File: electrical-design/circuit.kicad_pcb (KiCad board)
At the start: 4 copper layers, 90 x 70 mm, 53 parts, among them J1 AVR-ISP-6, Q1 2N3906, Q2 2N3906, Q3 2N3906, Q4 2N3906, SW1 Reset Button, SW2 DS02C-254-1L-04BE, SW3 Reset Button, U1 ATmega8A-P, U2 LTC-4627JR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

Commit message: Added Mechanical Design Folder
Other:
- board text added: "Villseriol Rev. 1.1"
- board text removed: "Rev 1.1"
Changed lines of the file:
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@@
       (layer "B.Paste" (type "Bottom Solder Paste"))
       (layer "B.SilkS" (type "Bottom Silk Screen"))
-      (copper_finish "HAL lead-free")
+      (copper_finish "None")
       (dielectric_constraints no)
     )
     (pad_to_mask_clearance 0)
+    (aux_axis_origin 60.96 27.94)
     (pcbplotparams
       (layerselection 0x00010fc_ffffffff)
@@
   (gr_line (start 104.648 71.628) (end 104.648 74.168)
     (stroke (width 0.1) (type solid)) (layer "F.SilkS"))
+  (gr_poly
+    (pts
+      (xy 131.534641 89.032925)
+      (xy 130.07684 89.032925)
+      (xy 130.07389 89.032839)
+      (xy 130.070968 89.032585)
+      (xy 130.06808 89.032164)
+      (xy 130.065232 89.031581)
+      (xy 130.06243 89.030839)
+      (xy 130.059682 89.02994)
+      (xy 130.056994 89.028888)
+      (xy 130.054371 89.027686)
+      (xy 130.051821 89.026337)
+      (xy 130.04935 89.024845)
+      (xy 130.046964 89.023212)
+      (xy 130.04467 89.021441)
+      (xy 130.042473 89.019537)
+      (xy 130.040382 89.017502)
+      (xy 130.038401 89.015338)
+      (xy 130.036537 89.01305)
+      (xy 130.03481 89.010658)
+      (xy 130.033233 89.008185)
+      (xy 130.031808 89.005638)
+      (xy 130.030536 89.003023)
+      (xy 130.02942 89.000349)
+      (xy 130.02846 88.997622)
+      (xy 130.027658 88.994848)
+      (xy 130.027015 88.992036)
+      (xy 130.026533 88.989192)
+      (xy 130.026213 88.986323)
+      (xy 130.026056 88.983436)
+      (xy 130.026063 88.980538)
+      (xy 130.026237 88.977636)
+      (xy 130.026579 88.974737)
+      (xy 130.027089 88.971849)
+      (xy 130.02777 88.968978)
+      (xy 130.175 88.419541)
+      (xy 131.064 88.419541)
+      (xy 131.392692 87.192827)
+      (xy 132.027692 87.192827)
+    )
+    (stroke (width 0) (type solid)) (fill solid) (layer "F.SilkS"))
+  (gr_poly
+    (pts
+      (xy 132.25282 86.427075)
+      (xy 132.25577 86.427161)
+      (xy 132.258692 86.427415)
+      (xy 132.26158 86.427836)
+      (xy 132.264428 86.428419)
+      (xy 132.26723 86.429161)
+      (xy 132.269978 86.43006)
+      (xy 132.272666 86.431112)
+      (xy 132.275289 86.432314)
+      (xy 132.277839 86.433663)
+      (xy 132.28031 86.435155)
+      (xy 132.282696 86.436788)
+      (xy 132.28499 86.438559)
+      (xy 132.287187 86.440463)
+      (xy 132.289278 86.442499)
+      (xy 132.291259 86.444662)
+      (xy 132.293123 86.44695)
+      (xy 132.294851 86.449342)
+      (xy 132.296428 86.451815)
+      (xy 132.297852 86.454362)
+      (xy 132.299124 86.456977)
+      (xy 132.30024 86.459651)
+      (xy 132.3012 86.462378)
+      (xy 132.302002 86.465152)
+      (xy 132.302645 86.467964)
+      (xy 132.303127 86.470808)
+      (xy 132.303447 86.473677)
+      (xy 132.303604 86.476564)
+      (xy 132.303597 86.479462)
+      (xy 132.303423 86.482364)
+      (xy 132.303081 86.485263)
+      (xy 132.302571 86.488151)
+      (xy 132.30189 86.491022)
+      (xy 132.15466 87.040459)
+      (xy 131.26566 87.040459)
+      (xy 130.936968 88.267173)
+      (xy 130.301968 88.267173)
+      (xy 130.795019 86.427075)
+    )
+    (stroke (width 0) (type solid)) (fill solid) (layer "F.SilkS"))
   (gr_circle (center 60.96 27.94) (end 61.96 27.94)
     (stroke (width 0.15) (type solid)) (fill none) (layer "Dwgs.User"))
@@
     (effects (font (size 0.75 0.75) (thickness 0.1)) (justify right bottom))
   )
-  (gr_text "Rev 1.1" (at 138.43 89.916) (layer "F.SilkS")
-    (effects (font (size 1 1) (thickness 0.15)) (justify right bottom))
+  (gr_text "Villseriol\nRev. 1.1" (at 133.35 88.9) (layer "F.SilkS")
+    (effects (font (size 0.75 0.75) (thickness 0.1)) (justify left bottom))
   )
   (gr_text "VCC" (at 141.732 64.008) (layer "F.SilkS")
@@
   (segment (start 94.850625 44.330625) (end 92.68 42.16) (width 0.2) (layer "In1.Cu") (net 24))
   (segment (start 94.850625 44.330625) (end 94.850625 46.736) (width 0.2) (layer "In1.Cu") (net 24))
-  (via (at 101.346 57.912) (size 0.475) (drill 0.2) (layers "F.Cu" "B.Cu") (net 25))
+  (via (at 101.346 57.912) (size 0.4) (drill 0.2) (layers "F.Cu" "B.Cu") (net 25))
   (segment (start 101.346 57.912) (end 74.422 57.912) (width 0.2) (layer "In1.Cu") (net 25))
   (segment (start 74.422 57.912) (end 70.104 53.594) (width 0.2) (layer "In1.Cu") (net 25))
@@
   (segment (start 101.346 57.912) (end 115.062 57.912) (width 0.2) (layer "In2.Cu") (net 25))
   (segment (start 123.847 56.388) (end 125.095 55.14) (width 0.2) (layer "In2.Cu") (net 25))
-  (via (at 101.346 57.15) (size 0.475) (drill 0.2) (layers "F.Cu" "B.Cu") (net 26))
+  (via (at 101.346 57.15) (size 0.4) (drill 0.2) (layers "F.Cu" "B.Cu") (net 26))
   (segment (start 101.346 57.15) (end 83.82 57.15) (width 0.2) (layer "In1.Cu") (net 26))
   (segment (start 83.82 57.15) (end 80.264 53.594) (width 0.2) (layer "In1.Cu") (net 26))
@@
   (segment (start 115.57 54.864) (end 116.586 53.848) (width 0.2) (layer "In2.Cu") (net 26))
   (segment (start 109.982 54.864) (end 115.57 54.864) (width 0.2) (layer "In2.Cu") (net 26))
-  (via (at 101.346 56.388) (size 0.475) (drill 0.2) (layers "F.Cu" "B.Cu") (net 27))
+  (via (at 101.346 56.388) (size 0.4) (drill 0.2) (layers "F.Cu" "B.Cu") (net 27))
   (segment (start 93.218 56.388) (end 90.424 53.594) (width 0.2) (layer "In1.Cu") (net 27))
   (segment (start 101.346 56.388) (end 93.218 56.388) (width 0.2) (layer "In1.Cu") (net 27))
@@
   (segment (start 107.442 56.388) (end 112.522 51.308) (width 0.2) (layer "In2.Cu") (net 27))
   (segment (start 112.522 51.308) (end 123.847 51.308) (width 0.2) (layer "In2.Cu") (net 27))
-  (via (at 101.346 55.626) (size 0.475) (drill 0.2) (layers "F.Cu" "B.Cu") (net 28))
+  (via (at 101.346 55.626) (size 0.4) (drill 0.2) (layers "F.Cu" "B.Cu") (net 28))
   (segment (start 100.584 54.864) (end 100.584 53.594) (width 0.2) (layer "In1.Cu") (net 28))
   (segment (start 101.346 55.626) (end 100.584 54.864) (width 0.2) (layer "In1.Cu") (net 28))
@@
   (segment (start 138.049 67.31) (end 134.747 67.31) (width 0.2) (layer "In2.Cu") (net 29))
   (segment (start 139.319 66.04) (end 138.049 67.31) (width 0.2) (layer "In2.Cu") (net 29))
-  (via (at 138.049 60.96) (size 0.475) (drill 0.2) (layers "F.Cu" "B.Cu") (net 30))
+  (via (at 138.049 60.96) (size 0.4) (drill 0.2) (layers "F.Cu" "B.Cu") (net 30))
   (segment (start 138.049 67.31) (end 136.779 68.58) (width 0.2) (layer "In1.Cu") (net 30))
   (segment (start 116.332 37.338) (end 114.046 35.052) (width 0.2) (layer "In1.Cu") (net 30))
@@
     )
   )
+  (group "" (id cf3e2b38-a358-478a-8d94-bbe55c8dc12f)
+    (members
+      e7582f17-23e3-469e-b44c-fc6a6f76012e
+      fa3fed59-9360-4068-a533-512832ddf0ab
+    )
+  )
+  (group "" (id d4487f5c-2c11-46ac-a5f1-d98bc9d2f5bd)
+    (members
+      769bce7a-d2b5-445b-93fd-8baec4745ac8
+      cf3e2b38-a358-478a-8d94-bbe55c8dc12f
+    )
+  )

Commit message: Completed Design of 1.2
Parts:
- SW2: value DS02C-254-1L-04BE -> SW_DIP_x04; footprint DIP Switch:DS02C2541L04BE -> Button_Switch_THT:SW_DIP_SPSTx04_Slide_9.78x12.34mm_W7.62mm_P2.54mm
- moved R12 18.4 mm to (84.8, 71.4)
- turned SW2 to 90 degrees
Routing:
- net Net-(R12-Pad2): track 7.51 -> 14.3 mm
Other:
- board text added: "Villseriol Rev. 1.2"
- board text removed: "Villseriol Rev. 1.1"

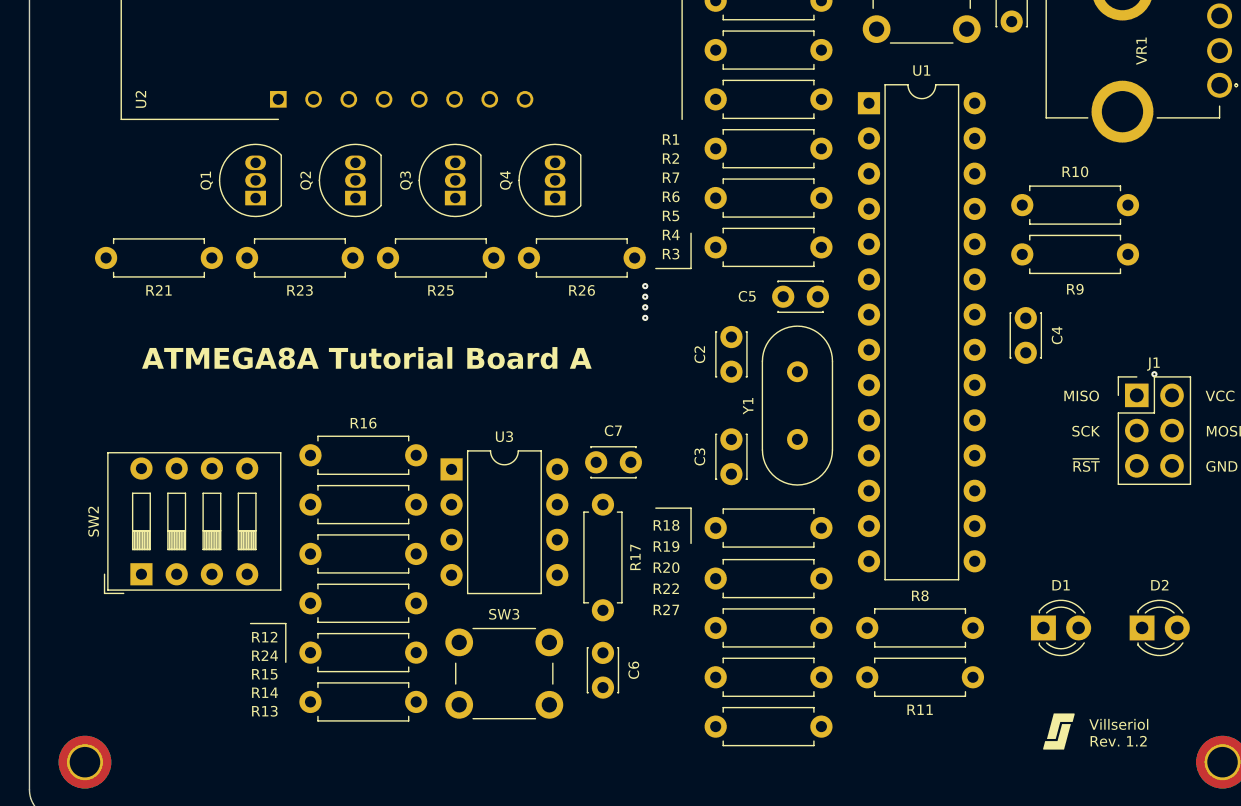
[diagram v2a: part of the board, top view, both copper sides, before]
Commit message: Made DIP Packages Use Socket
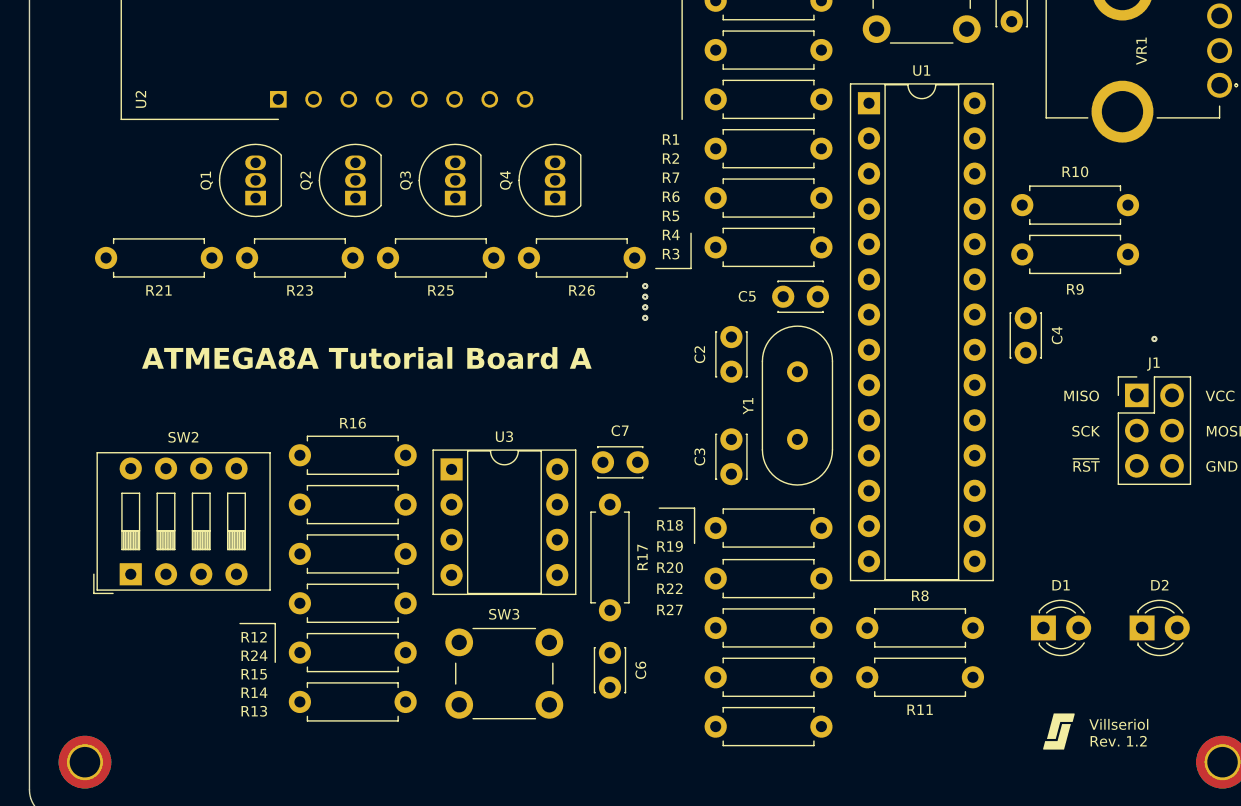
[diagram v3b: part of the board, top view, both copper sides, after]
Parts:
- U1: footprint Package_DIP:DIP-28_W7.62mm -> Package_DIP:DIP-28_W7.62mm_Socket
- U3: footprint Package_DIP:DIP-8_W7.62mm -> Package_DIP:DIP-8_W7.62mm_Socket
- moved SW2 0.77 mm to (64.3, 76.4)
- moved R12 0.76 mm to (84.1, 71.4)
- moved R13 0.76 mm to (84.1, 85.6)
- moved R14 0.76 mm to (84.1, 82.0)
- moved R15 0.76 mm to (84.1, 78.5)
- moved R16 0.76 mm to (76.5, 67.8)
- moved R24 0.76 mm to (76.5, 74.9)
- moved C6 0.51 mm to (98.8, 82.1)
- moved R17 0.51 mm to (98.8, 71.4)
- moved C7 0.49 mm to (98.3, 68.3)
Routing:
- net Net-(U3-DIS): track 38.6 -> 40.3 mm
